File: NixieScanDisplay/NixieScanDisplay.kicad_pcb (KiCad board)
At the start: 2 copper layers, 156.5 x 67.5 mm, 104 parts, among them J1 Conn_01x07, J2 Conn_01x01, J3 Conn_01x01, J4 Conn_01x01, J5 Conn_01x01, Q1 2N2222A, Q10 MPSA42, Q11 MPSA42, Q12 MPSA42, Q13 MPSA42, Q14 MPSA42, Q15 MPSA92, Q16 MPSA42, Q17 MPSA42, Q18 MPSA92, Q19 MPSA42, Q2 IRF840, Q20 MPSA42, Q21 MPSA42, Q22 MPSA92, Q23 MPSA42, Q24 MPSA92, Q25 MPSA42, Q26 MPSA92, Q3 MPSA42, Q4 MPSA42, Q5 MPSA42, Q6 MPSA42, Q7 MPSA92, Q8 MPSA42, Q9 MPSA42, U1 NE555, U2 L7805, U3 74HC595, U4 74HC595, U5 74HC595

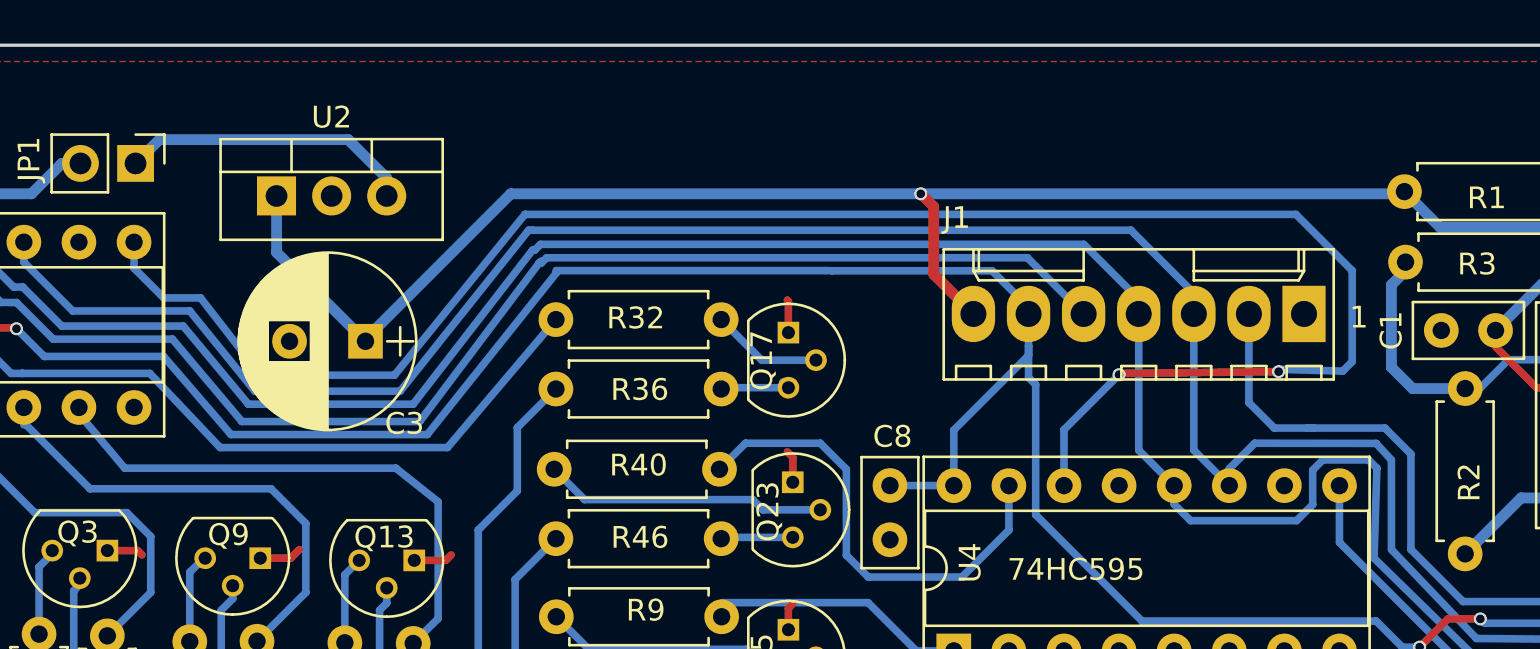
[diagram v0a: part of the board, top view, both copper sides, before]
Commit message: Placed connectors to make boards stackable
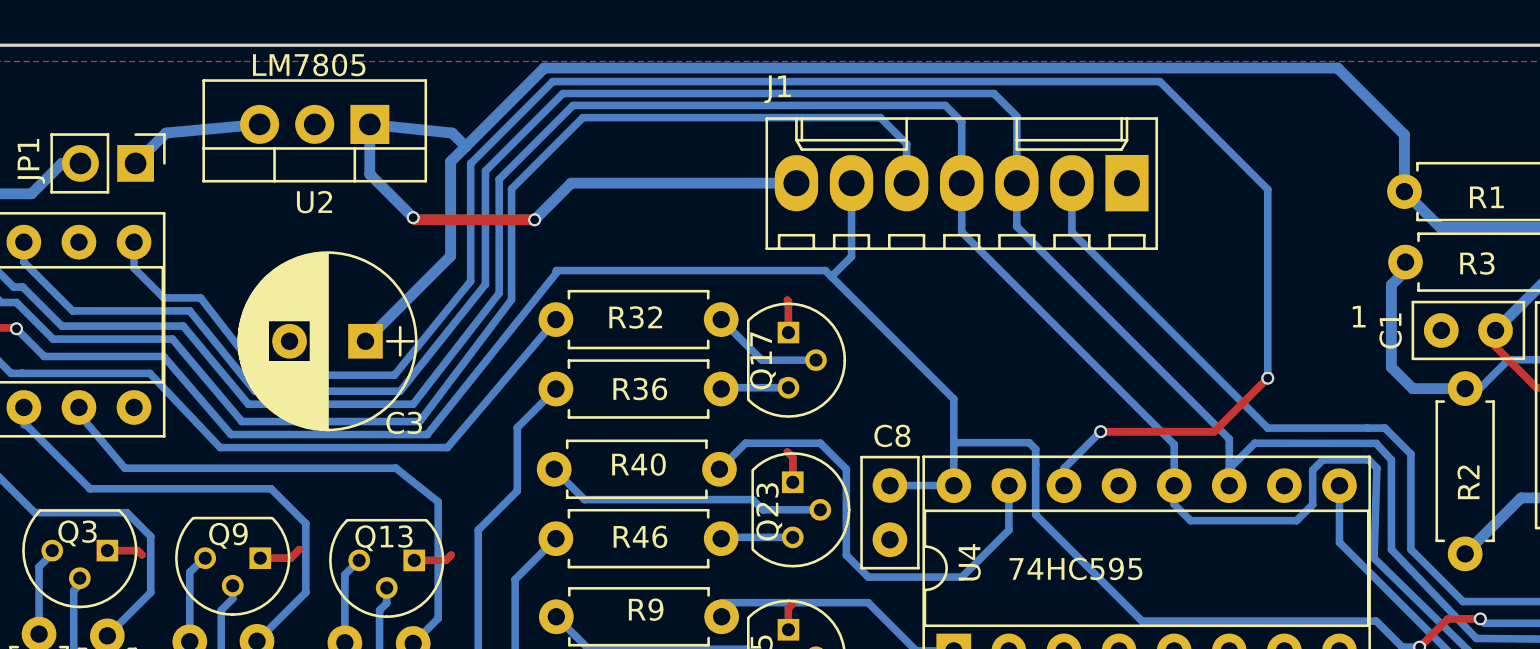
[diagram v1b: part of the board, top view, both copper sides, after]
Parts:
- moved J1 10.1 mm to (194.4, 55.2)
- moved U2 5.42 mm to (159.5, 52.5), turned to 180 degrees
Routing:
- net +12V: track 110.9 -> 133.2 mm, vias 1 -> 2
- net SERDATAOUT: track 80.0 -> 89.3 mm
- net SERLATCH: track 146.0 -> 154.2 mm
- net SERCLK: track 145.0 -> 153.1 mm
- net Net-(JP1-Pad1): track 13.6 -> 6.32 mm
- net +5V: track 181.9 -> 178.3 mm
- net Net-(U3-Pad9): track 85.6 -> 87.5 mm
- net SERDATA: track 66.0 -> 64.4 mm
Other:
- board text added: "LM7805"

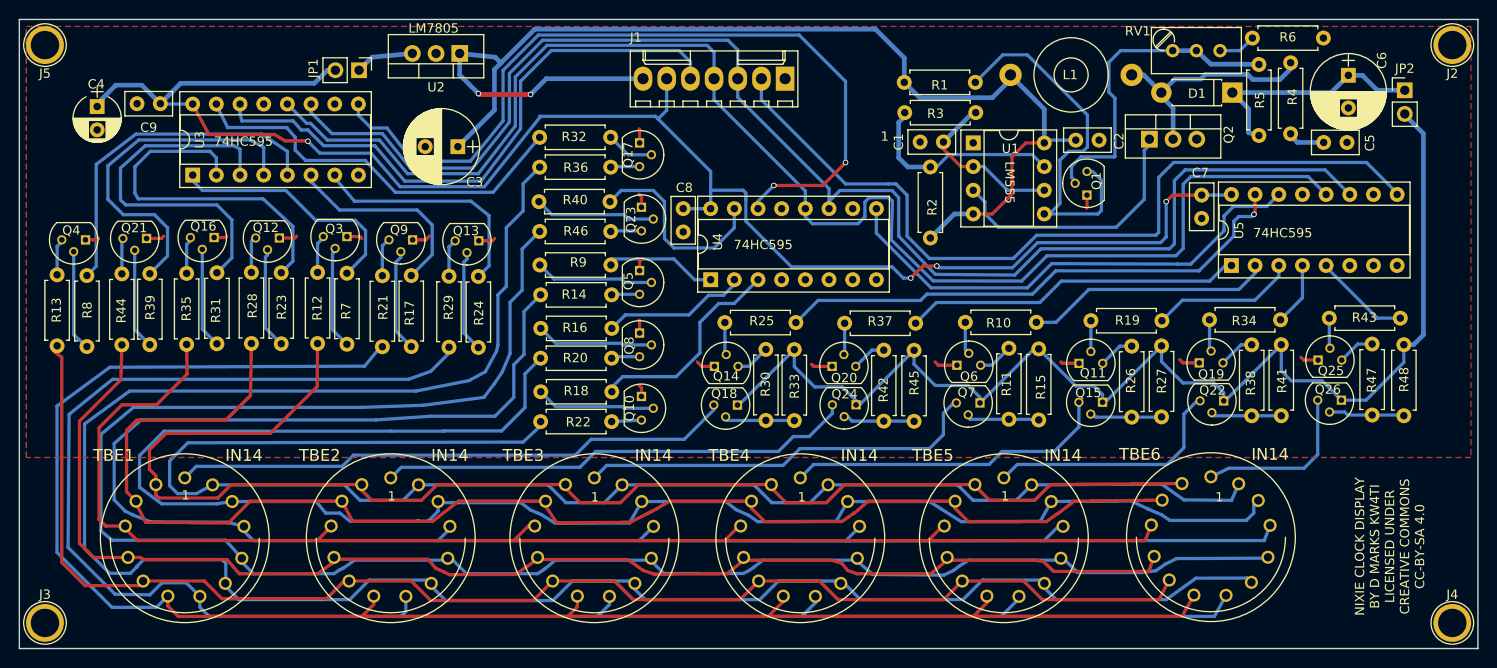
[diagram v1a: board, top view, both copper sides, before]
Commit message: First usable version of Nixie Tube Clock
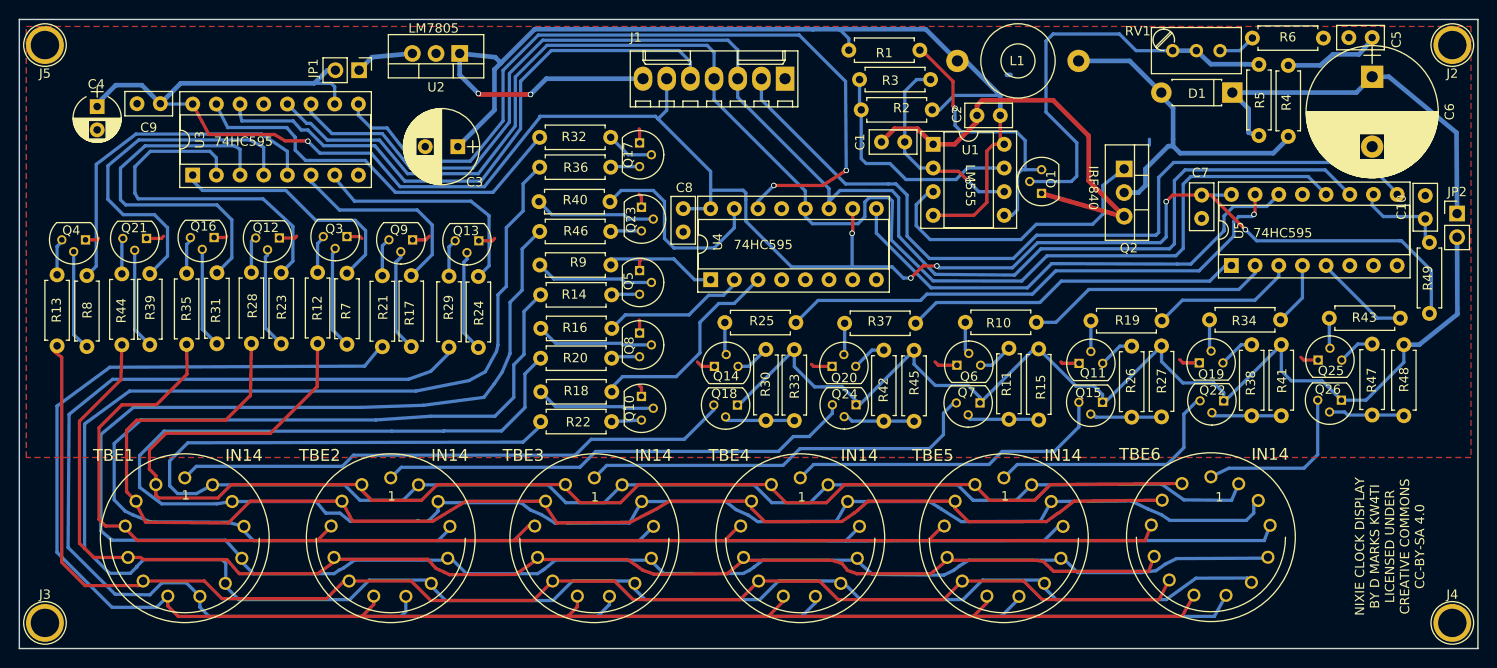
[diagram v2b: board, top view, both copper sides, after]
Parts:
- added C10: 100 nF, Capacitors_THT:C_Disc_D5.0mm_W2.5mm_P2.50mm, F.Cu at (263.1, 70.2)
- added R49: 10k, Resistors_THT:R_Axial_DIN0207_L6.3mm_D2.5mm_P7.62mm_Horizontal, F.Cu at (263.6, 80.4)
- C6: footprint Capacitors_THT:CP_Radial_D8.0mm_P3.50mm -> Capacitors_THT:CP_Radial_D14.0mm_P7.50mm
- R12, R22: value 680k -> 22k
- R13, R14, R20, R21, R28, R29, R35, R36, R44, R46: value 180k -> 10k
- moved JP2 14.4 mm to (266.5, 69.7)
- moved R2 13.8 mm to (210.2, 58.5), turned to 180 degrees
- moved C5 12.4 mm to (257.4, 50.8), turned to 180 degrees
- moved C2 8.52 mm to (217.5, 59.1), turned to 180 degrees
- moved R4 7.90 mm to (248.4, 61.4), turned to 90 degrees
- moved R1 6.88 mm to (201.2, 52.1)
- moved R3 6.01 mm to (202.4, 55.3)
- moved L1 5.89 mm to (212.9, 53.3)
- moved Q1 4.87 mm to (221.9, 67.5)
- moved U1 4.30 mm to (210.3, 62.2)
- moved Q2 4.18 mm to (230.8, 64.9), turned to 270 degrees
- moved C1 4.15 mm to (207.2, 62.0)
- moved C6 2.55 mm to (257.4, 55.0)
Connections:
- U3 pad 10: (no net) -> +5V
- U3 pad 13: (no net) -> GND
- U4 pad 10: (no net) -> +5V
- U4 pad 13: (no net) -> GND
- U5 pad 10: (no net) -> Net-(C10-Pad1)
- U5 pad 13: (no net) -> GND
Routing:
- net GND: track 33.7 -> 79.9 mm
- net +5V: track 178.3 -> 221.4 mm, vias 4 -> 6
- net Net-(C6-Pad1): track 26.1 -> 41.8 mm
- net Net-(D1-Pad2): track 25.5 -> 38.4 mm
- net NIXIEPWR: track 132.7 -> 120.8 mm
- net Net-(Q1-Pad2): track 34.6 -> 45.6 mm
- net Net-(Q1-Pad3): track 41.2 -> 30.4 mm, vias 0 -> 1
- net Net-(C10-Pad1): track 0.00 -> 10.7 mm
- net Net-(C5-Pad1): track 4.04 -> 11.0 mm
- net +12V: track 133.2 -> 127.9 mm
- net Net-(C1-Pad1): track 18.2 -> 22.3 mm, vias 0 -> 1
- net Net-(Q2-Pad1): track 28.7 -> 32.4 mm
- net Net-(R2-Pad2): track 22.2 -> 25.3 mm
- net (no net): track 0.00 -> 1.41 mm
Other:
- board text added: "IRF840"

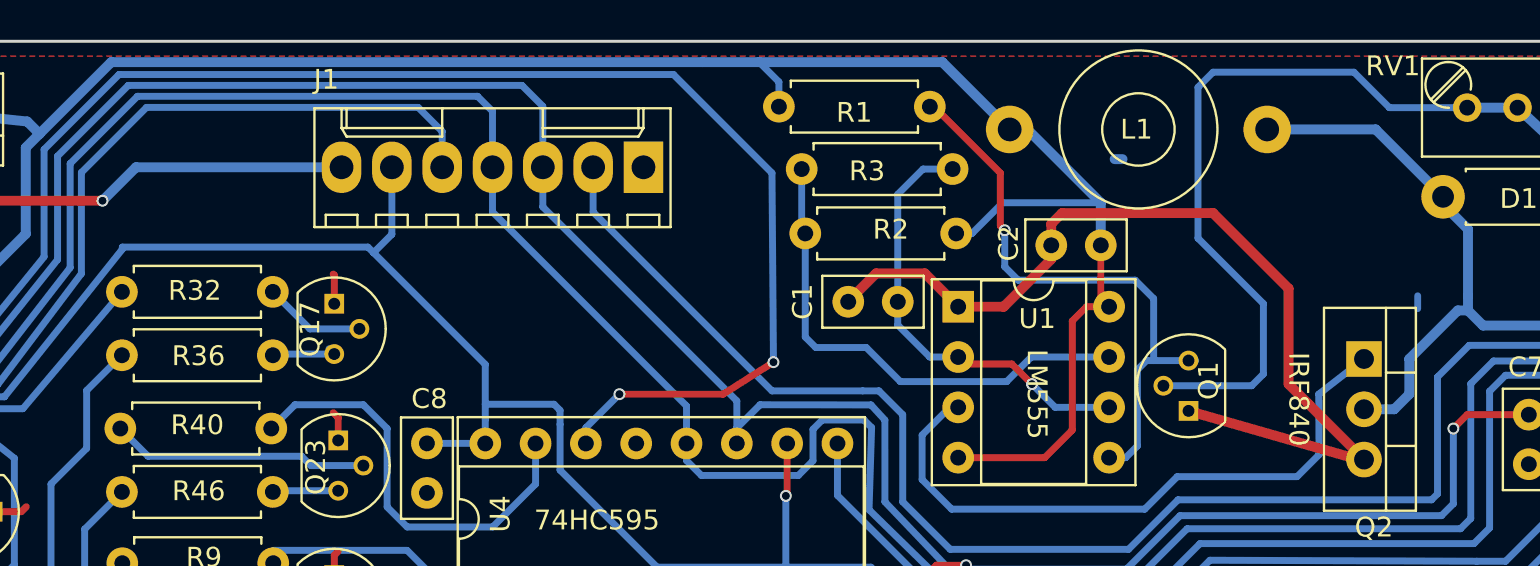
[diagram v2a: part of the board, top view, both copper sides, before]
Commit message: Changed connector between boards to 10 pin IDC, added Bill of Materials
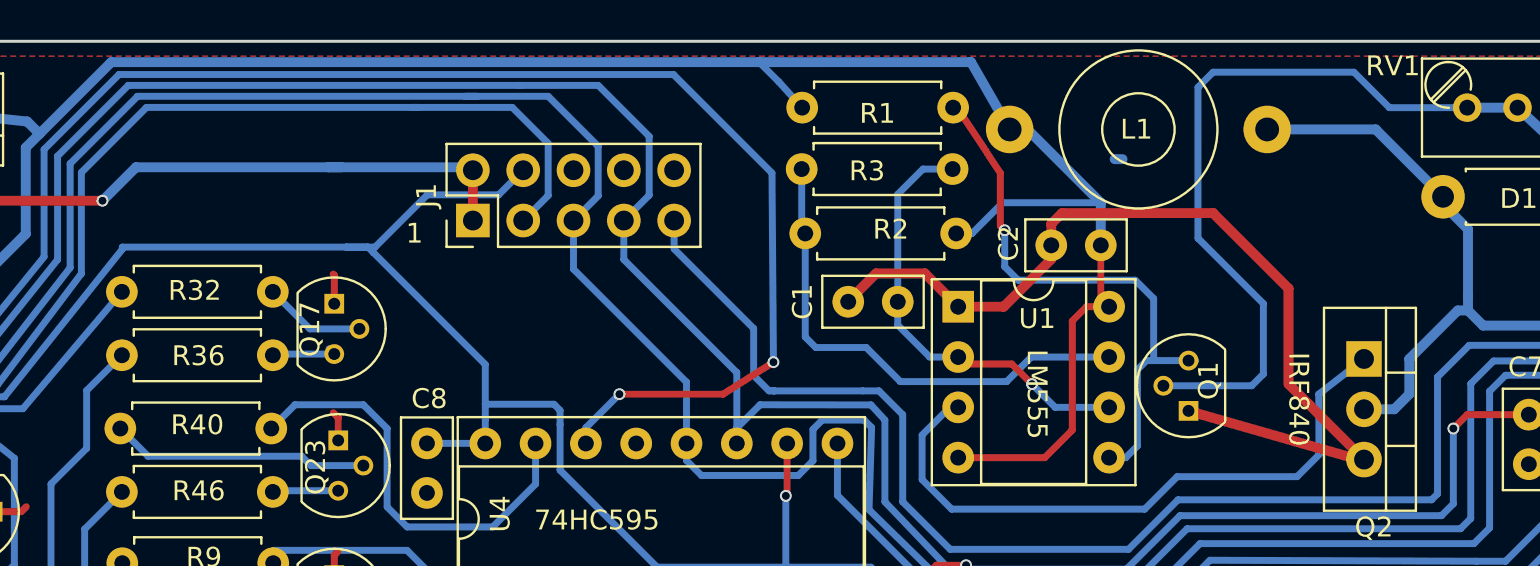
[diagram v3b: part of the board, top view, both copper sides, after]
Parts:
- J1: value Conn_01x07 -> Conn_02x05_Odd_Even; footprint Connectors_Molex:Molex_KK-6410-07_07x2.54mm_Straight -> Pin_Headers:Pin_Header_Straight_2x05_Pitch2.54mm
- moved J1 9.02 mm to (185.8, 57.9), turned to 90 degrees
- moved R1 1.18 mm to (202.4, 52.2)
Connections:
- J1 pad 1: GND -> +12V
- J1 pad 2: SERDATAOUT -> +12V
- J1 pad 3: SERCLK -> SERDATA
- J1 pad 4: SERLATCH -> +5V
- J1 pad 5: SERDATA -> SERLATCH
- J1 pad 6: +5V -> GND
- J1 pad 7: +12V -> SERCLK
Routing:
- net +12V: track 127.9 -> 138.8 mm
- net SERDATA: track 64.4 -> 73.0 mm
- net +5V: track 221.4 -> 227.3 mm
- net SERDATAOUT: track 89.3 -> 85.2 mm
- net SERLATCH: track 154.2 -> 158.0 mm
- net SERCLK: track 153.1 -> 156.6 mm
- net Net-(Q1-Pad3): track 30.4 -> 29.6 mm
- net (no net): track 1.41 -> 0.76 mm
